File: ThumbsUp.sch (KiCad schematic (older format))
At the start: 138 parts, among them J1 Conn_01x04_Male, J10 Raiser_Male, J11 Raiser_Female, J12 Raiser_Male, J13 Raiser_Female, J14 Raiser_Male, J15 Raiser_Female, J16 Raiser_Male, J17 Raiser_Female, J18 Raiser_Male, J19 52559-1233, J2 Conn_01x04_Male, J20 Conn_01x04_Female, J21 Conn_01x04_Female, J22 Conn_01x04_Female, J23 Conn_01x04_Female, J24 Conn_01x04_Male, J25 Conn_01x04_Male, J26 Conn_01x04_Male, J27 Conn_01x04_Male, J28 Conn_01x04_Female, J29 Conn_01x04_Female, J3 Conn_01x04_Female, J30 Conn_01x04_Female, J31 Conn_01x04_Female, J4 Conn_01x04_Male, J5 Conn_01x04_Female, J6 Conn_01x04_Male, J7 Conn_01x04_Male, J8 Conn_01x04_Male, J9 Raiser_Female, SW1 SW_Push, U1 ATmega32U4-AU, Y1 16MHz

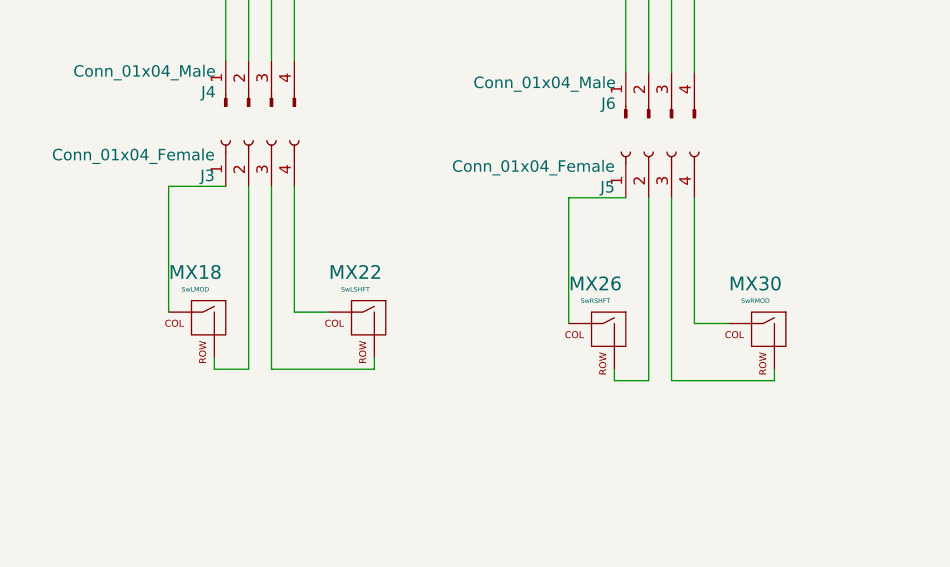
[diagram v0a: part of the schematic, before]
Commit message: Swapped space and shift keys
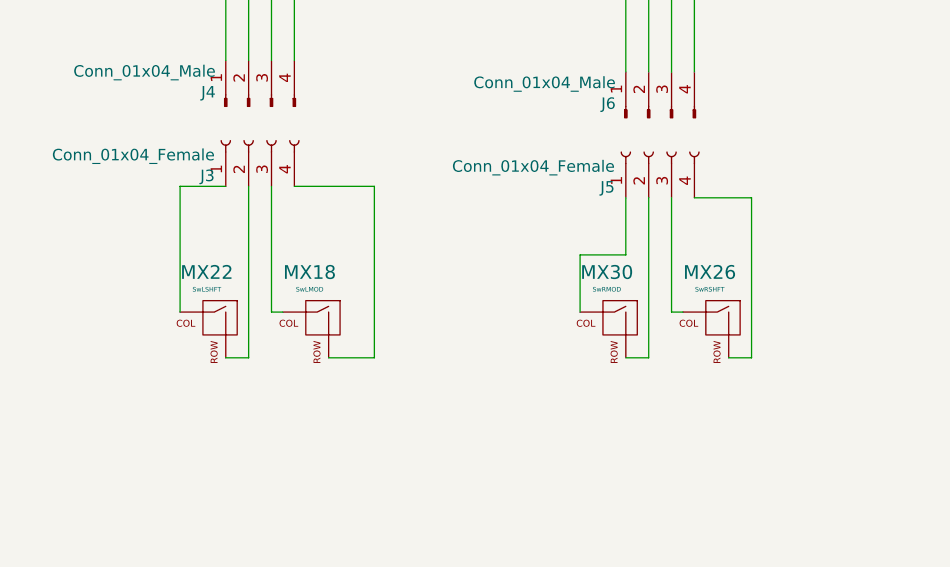
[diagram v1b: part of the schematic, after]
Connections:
- net at MX22.1 (COL): now also J3.1 (Pin_1); no longer J3.4 (Pin_4)
- net at MX22.2 (ROW): now also J3.2 (Pin_2); no longer J3.3 (Pin_3)
- net at MX18.1 (COL): now also J3.3 (Pin_3); no longer J3.1 (Pin_1)
- net at MX18.2 (ROW): now also J3.4 (Pin_4); no longer J3.2 (Pin_2)
- net at MX30.1 (COL): now also J5.1 (Pin_1); no longer J5.4 (Pin_4)
- net at MX30.2 (ROW): now also J5.2 (Pin_2); no longer J5.3 (Pin_3)
- net at MX26.1 (COL): now also J5.3 (Pin_3); no longer J5.1 (Pin_1)
- net at MX26.2 (ROW): now also J5.4 (Pin_4); no longer J5.2 (Pin_2)
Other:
- moved on the sheet: MX18, MX22, MX26, MX30
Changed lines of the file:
@@
 	0    1    1    0
 $EndComp
-Wire Wire Line
-	4200 4350 4100 4350
 $Comp
 L Device:R_Small R2
@@
 NoConn ~ 2050 2550
 $Comp
-L Device:C_Small C3
-U 1 1 61D27F3E
-P 1600 4450
-F 0 "C3" H 1692 4496 50  0000 L CNN
-F 1 "1uF" H 1692 4405 50  0000 L CNN
-F 2 "Capacitor_SMD:C_0805_2012Metric" H 1600 4450 50  0001 C CNN
-F 3 "~" H 1600 4450 50  0001 C CNN
-	1    1600 4450
-	1    0    0    -1
-$EndComp
-$Comp
 L power:+5V #PWR018
 U 1 1 61D515F6
@@
 $EndComp
 $Comp
-L power:VCC #PWR04
-U 1 1 61D6313F
-P 2000 5200
-F 0 "#PWR04" H 2000 5050 50  0001 C CNN
-F 1 "VCC" H 2017 5373 50  0000 C CNN
-F 2 "" H 2000 5200 50  0001 C CNN
-F 3 "" H 2000 5200 50  0001 C CNN
-	1    2000 5200
-	1    0    0    -1
-$EndComp
-$Comp
 L power:+5V #PWR01
 U 1 1 61D69604
@@
 F 3 "" H 1600 4350 50  0001 C CNN
 	1    1600 4350
-	1    0    0    -1
-$EndComp
-$Comp
-L power:GND #PWR02
-U 1 1 61D6A039
-P 1600 4550
-F 0 "#PWR02" H 1600 4300 50  0001 C CNN
-F 1 "GND" H 1605 4377 50  0000 C CNN
-F 2 "" H 1600 4550 50  0001 C CNN
-F 3 "" H 1600 4550 50  0001 C CNN
-	1    1600 4550
 	1    0    0    -1
 $EndComp
@@
 L ThumbsUp-rescue:MX-NoLED-MX_Alps_Hybrid MX22
 U 1 1 62882FE4
-P 8850 11000
-F 0 "MX22" H 8883 11223 60  0000 C CNN
-F 1 "SwLSHFT" H 8883 11149 20  0000 C CNN
-F 2 "keyswitches:Kailh_socket_PG1350_optional" H 8225 10975 60  0001 C CNN
-F 3 "" H 8225 10975 60  0001 C CNN
-	1    8850 11000
+P 8200 11000
+F 0 "MX22" H 8233 11223 60  0000 C CNN
+F 1 "SwLSHFT" H 8233 11149 20  0000 C CNN
+F 2 "keyswitches:Kailh_socket_PG1350_optional" H 7575 10975 60  0001 C CNN
+F 3 "" H 7575 10975 60  0001 C CNN
+	1    8200 11000
 	-1   0    0    -1
 $EndComp
@@
 L ThumbsUp-rescue:MX-NoLED-MX_Alps_Hybrid MX18
 U 1 1 62882FEA
-P 8150 11000
-F 0 "MX18" H 8183 11223 60  0000 C CNN
-F 1 "SwLMOD" H 8183 11149 20  0000 C CNN
-F 2 "keyswitches:Kailh_socket_PG1350_optional" H 7525 10975 60  0001 C CNN
-F 3 "" H 7525 10975 60  0001 C CNN
-	1    8150 11000
+P 8650 11000
+F 0 "MX18" H 8683 11223 60  0000 C CNN
+F 1 "SwLMOD" H 8683 11149 20  0000 C CNN
+F 2 "keyswitches:Kailh_socket_PG1350_optional" H 8025 10975 60  0001 C CNN
+F 3 "" H 8025 10975 60  0001 C CNN
+	1    8650 11000
 	-1   0    0    -1
 $EndComp
-Wire Wire Line
-	8200 11200 8200 11150
 $Comp
 L Connector:Conn_01x04_Female J3
@@
 	0    -1   -1   0
 $EndComp
-Wire Wire Line
-	8250 10400 8000 10400
-Wire Wire Line
-	8000 10400 8000 10950
-Wire Wire Line
-	8350 10400 8350 11200
-Wire Wire Line
-	8350 11200 8200 11200
-Wire Wire Line
-	8450 10400 8450 11200
-Wire Wire Line
-	8450 11200 8900 11200
-Wire Wire Line
-	8900 11200 8900 11150
-Wire Wire Line
-	8550 10400 8550 10950
-Wire Wire Line
-	8550 10950 8700 10950
 $Comp
 L ThumbsUp-rescue:MX-NoLED-MX_Alps_Hybrid MX30
 U 1 1 62A1D5C7
-P 10600 11050
-F 0 "MX30" H 10633 11273 60  0000 C CNN
-F 1 "SwRMOD" H 10633 11199 20  0000 C CNN
-F 2 "keyswitches:Kailh_socket_PG1350_optional" H 9975 11025 60  0001 C CNN
-F 3 "" H 9975 11025 60  0001 C CNN
-	1    10600 11050
+P 9950 11000
+F 0 "MX30" H 9983 11223 60  0000 C CNN
+F 1 "SwRMOD" H 9983 11149 20  0000 C CNN
+F 2 "keyswitches:Kailh_socket_PG1350_optional" H 9325 10975 60  0001 C CNN
+F 3 "" H 9325 10975 60  0001 C CNN
+	1    9950 11000
 	-1   0    0    -1
 $EndComp
@@
 L ThumbsUp-rescue:MX-NoLED-MX_Alps_Hybrid MX26
 U 1 1 62A1D5CD
-P 9900 11050
-F 0 "MX26" H 9933 11273 60  0000 C CNN
-F 1 "SwRSHFT" H 9933 11199 20  0000 C CNN
-F 2 "keyswitches:Kailh_socket_PG1350_optional" H 9275 11025 60  0001 C CNN
-F 3 "" H 9275 11025 60  0001 C CNN
-	1    9900 11050
+P 10400 11000
+F 0 "MX26" H 10433 11223 60  0000 C CNN
+F 1 "SwRSHFT" H 10433 11149 20  0000 C CNN
+F 2 "keyswitches:Kailh_socket_PG1350_optional" H 9775 10975 60  0001 C CNN
+F 3 "" H 9775 10975 60  0001 C CNN
+	1    10400 11000
 	-1   0    0    -1
 $EndComp
-Wire Wire Line
-	9950 11250 9950 11200
 $Comp
 L Connector:Conn_01x04_Female J5
@@
 	0    -1   -1   0
 $EndComp
-Wire Wire Line
-	10000 10450 9750 10450
-Wire Wire Line
-	9750 10450 9750 11000
-Wire Wire Line
-	10100 10450 10100 11250
-Wire Wire Line
-	10100 11250 9950 11250
-Wire Wire Line
-	10200 10450 10200 11250
-Wire Wire Line
-	10200 11250 10650 11250
-Wire Wire Line
-	10650 11250 10650 11200
-Wire Wire Line
-	10300 10450 10300 11000
-Wire Wire Line
-	10300 11000 10450 11000
 Wire Wire Line
 	7750 9200 8350 9200
@@
 Text GLabel 4200 3550 2    50   Input ~ 0
 SDA
-Connection ~ 4200 4350
 Wire Wire Line
 	4650 4350 4750 4350
-Wire Wire Line
-	4450 4350 4200 4350
-$Comp
-L MCU_Microchip_ATmega:ATmega32U4-AU U1
-U 1 1 616A381E
-P 3600 3750
-F 0 "U1" H 3600 1861 50  0000 C CNN
-F 1 "ATmega32U4-AU" H 3600 1770 50  0000 C CNN
-F 2 "Package_QFP:TQFP-44_10x10mm_P0.8mm" H 3600 3750 50  0001 C CIN
-F 3 "http://ww1.microchip.com/downloads/en/DeviceDoc/Atmel-7766-8-bit-AVR-ATmega16U4-32U4_Datasheet.pdf" H 3600 3750 50  0001 C CNN
-	1    3600 3750
-	1    0    0    -1
-$EndComp
 Text GLabel 9550 4450 3    50   Input ~ 0
 SDA
@@
 NoConn ~ 10900 4050
 Wire Wire Line
-	3050 5550 3500 5550
-Connection ~ 3500 5550
-Wire Wire Line
-	3500 5550 3600 5550
-Wire Wire Line
 	3700 1550 3700 1950
 Wire Wire Line
 	3700 1950 3600 1950
-Connection ~ 3700 1950
 Wire Wire Line
 	1750 5550 2150 5550
@@
 GND-TOP
 NoConn ~ 9300 2750
+Connection ~ 3700 1950
+Connection ~ 3500 5550
+Wire Wire Line
+	3500 5550 3600 5550
+Wire Wire Line
+	3050 5550 3500 5550
+Connection ~ 4200 4350
+Wire Wire Line
+	4450 4350 4200 4350
+Wire Wire Line
+	4200 4350 4100 4350
+$Comp
+L MCU_Microchip_ATmega:ATmega32U4-AU U1
+U 1 1 616A381E
+P 3600 3750
+F 0 "U1" H 3600 1861 50  0000 C CNN
+F 1 "ATmega32U4-AU" H 3600 1770 50  0000 C CNN
+F 2 "Package_QFP:TQFP-44_10x10mm_P0.8mm" H 3600 3750 50  0001 C CIN
+F 3 "http://ww1.microchip.com/downloads/en/DeviceDoc/Atmel-7766-8-bit-AVR-ATmega16U4-32U4_Datasheet.pdf" H 3600 3750 50  0001 C CNN
+	1    3600 3750
+	1    0    0    -1
+$EndComp
+$Comp
+L power:GND #PWR02
+U 1 1 61D6A039
+P 1600 4550
+F 0 "#PWR02" H 1600 4300 50  0001 C CNN
+F 1 "GND" H 1605 4377 50  0000 C CNN
+F 2 "" H 1600 4550 50  0001 C CNN
+F 3 "" H 1600 4550 50  0001 C CNN
+	1    1600 4550
+	1    0    0    -1
+$EndComp
+$Comp
+L power:VCC #PWR04
+U 1 1 61D6313F
+P 2000 5200
+F 0 "#PWR04" H 2000 5050 50  0001 C CNN
+F 1 "VCC" H 2017 5373 50  0000 C CNN
+F 2 "" H 2000 5200 50  0001 C CNN
+F 3 "" H 2000 5200 50  0001 C CNN
+	1    2000 5200
+	1    0    0    -1
+$EndComp
+$Comp
+L Device:C_Small C3
+U 1 1 61D27F3E
+P 1600 4450
+F 0 "C3" H 1692 4496 50  0000 L CNN
+F 1 "1uF" H 1692 4405 50  0000 L CNN
+F 2 "Capacitor_SMD:C_0805_2012Metric" H 1600 4450 50  0001 C CNN
+F 3 "~" H 1600 4450 50  0001 C CNN
+	1    1600 4450
+	1    0    0    -1
+$EndComp
+Wire Wire Line
+	8250 10400 8050 10400
+Wire Wire Line
+	8050 10400 8050 10950
+Wire Wire Line
+	8250 11150 8350 11150
+Wire Wire Line
+	8350 11150 8350 10400
+Wire Wire Line
+	8500 10950 8450 10950
+Wire Wire Line
+	8450 10950 8450 10400
+Wire Wire Line
+	8700 11150 8900 11150
+Wire Wire Line
+	8900 11150 8900 10400
+Wire Wire Line
+	8900 10400 8550 10400
+Wire Wire Line
+	10000 11150 10100 11150
+Wire Wire Line
+	10100 11150 10100 10450
+Wire Wire Line
+	10250 10950 10200 10950
+Wire Wire Line
+	10200 10950 10200 10450
+Wire Wire Line
+	9800 10950 9800 10700
+Wire Wire Line
+	9800 10700 10000 10700
+Wire Wire Line
+	10000 10700 10000 10450
+Wire Wire Line
+	10450 11150 10550 11150
+Wire Wire Line
+	10550 11150 10550 10450
+Wire Wire Line
+	10550 10450 10300 10450
 $EndSCHEMATC

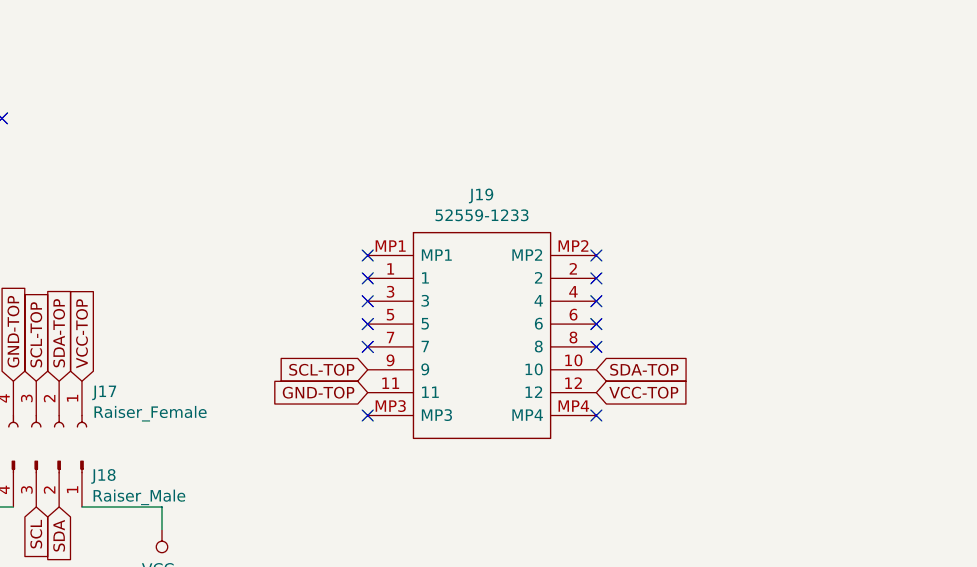
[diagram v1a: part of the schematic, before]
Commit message: Added pullup resistors for trackpad, re-produced the gerbers
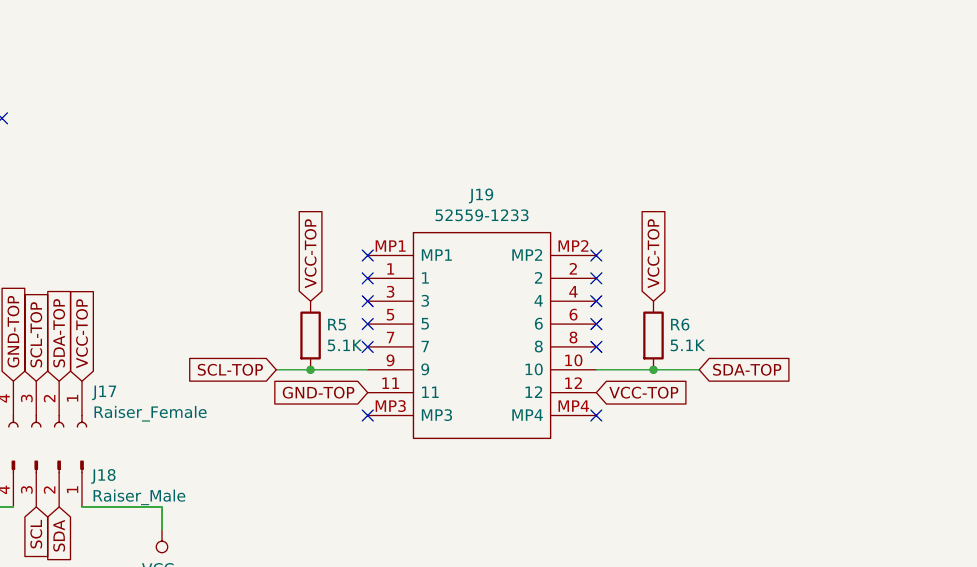
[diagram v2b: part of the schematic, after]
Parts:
- added R5, R6: 5.1K, Resistor_SMD:R_0805_2012Metric, symbol Device:R
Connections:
- net SCL-TOP: now also R5.2
- net SDA-TOP: now also R6.2
- net VCC-TOP: now also R5.1, R6.1
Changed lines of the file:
@@
 	1    0    0    -1
 $EndComp
-Text GLabel 10900 3850 0    50   Input ~ 0
+Text GLabel 10500 3850 0    50   Input ~ 0
 SCL-TOP
-Text GLabel 11900 3850 2    50   Input ~ 0
+Text GLabel 12350 3850 2    50   Input ~ 0
 SDA-TOP
 Text GLabel 4200 3450 2    50   Input ~ 0
@@
 Wire Wire Line
 	10550 10450 10300 10450
+$Comp
+L Device:R R6
+U 1 1 63A12574
+P 12150 3700
+F 0 "R6" H 12220 3746 50  0000 L CNN
+F 1 "5.1K" H 12220 3655 50  0000 L CNN
+F 2 "Resistor_SMD:R_0805_2012Metric" V 12080 3700 50  0001 C CNN
+F 3 "~" H 12150 3700 50  0001 C CNN
+	1    12150 3700
+	1    0    0    -1
+$EndComp
+$Comp
+L Device:R R5
+U 1 1 63A138DC
+P 10650 3700
+F 0 "R5" H 10720 3746 50  0000 L CNN
+F 1 "5.1K" H 10720 3655 50  0000 L CNN
+F 2 "Resistor_SMD:R_0805_2012Metric" V 10580 3700 50  0001 C CNN
+F 3 "~" H 10650 3700 50  0001 C CNN
+	1    10650 3700
+	1    0    0    -1
+$EndComp
+Wire Wire Line
+	10500 3850 10650 3850
+Connection ~ 10650 3850
+Wire Wire Line
+	10650 3850 10900 3850
+Wire Wire Line
+	11900 3850 12150 3850
+Connection ~ 12150 3850
+Wire Wire Line
+	12150 3850 12350 3850
+Text GLabel 12150 3550 1    50   Input ~ 0
+VCC-TOP
+Text GLabel 10650 3550 1    50   Input ~ 0
+VCC-TOP
 $EndSCHEMATC
